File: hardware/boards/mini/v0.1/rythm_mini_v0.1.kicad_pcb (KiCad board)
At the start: 8 copper layers, 18 x 50 mm, 62 parts, among them IC1 NAU88C22YG, IC2 IS42S32160F-6BLI, U1 W25Q128JVP, U2 LTV-217-G, U3 RythmMini, U7 STM32H750IBKx, Y2 Crystal_GND24

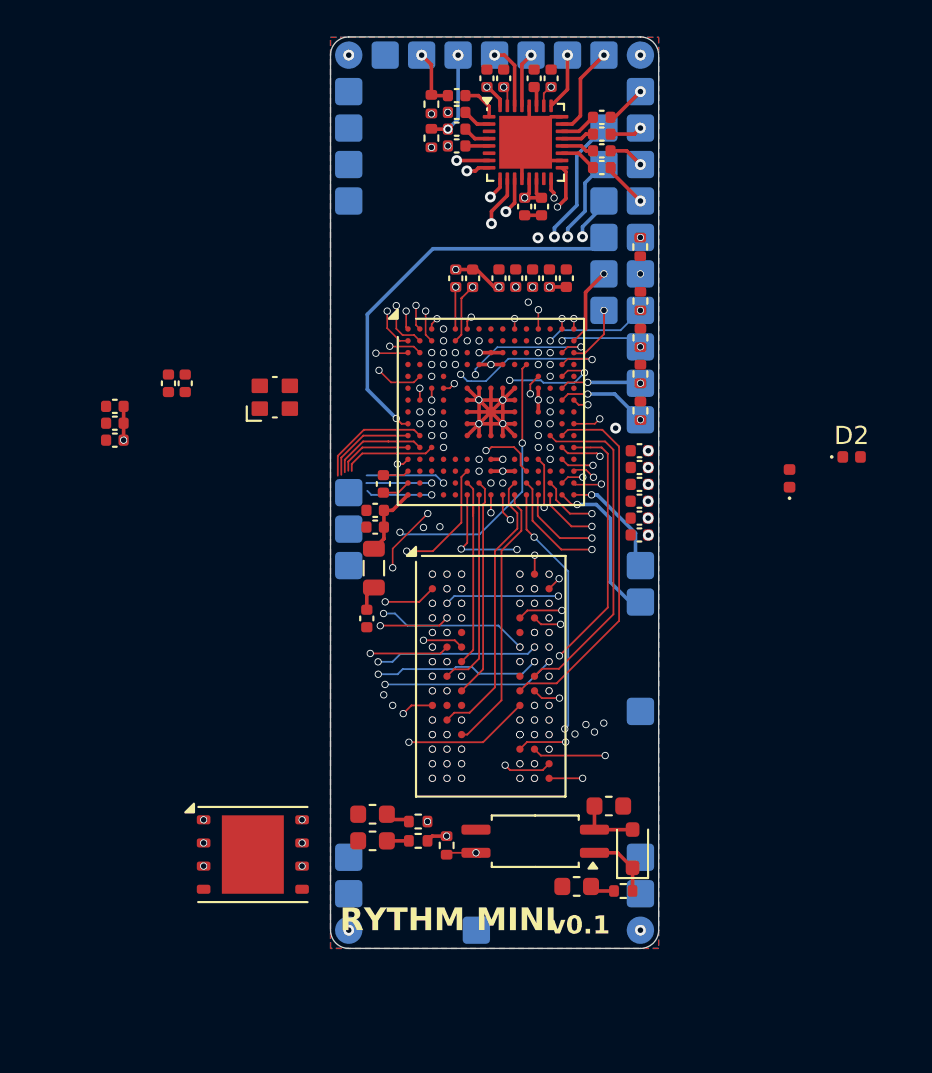
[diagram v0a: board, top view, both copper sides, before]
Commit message: mini: route qspi flash and add more brakeout pads
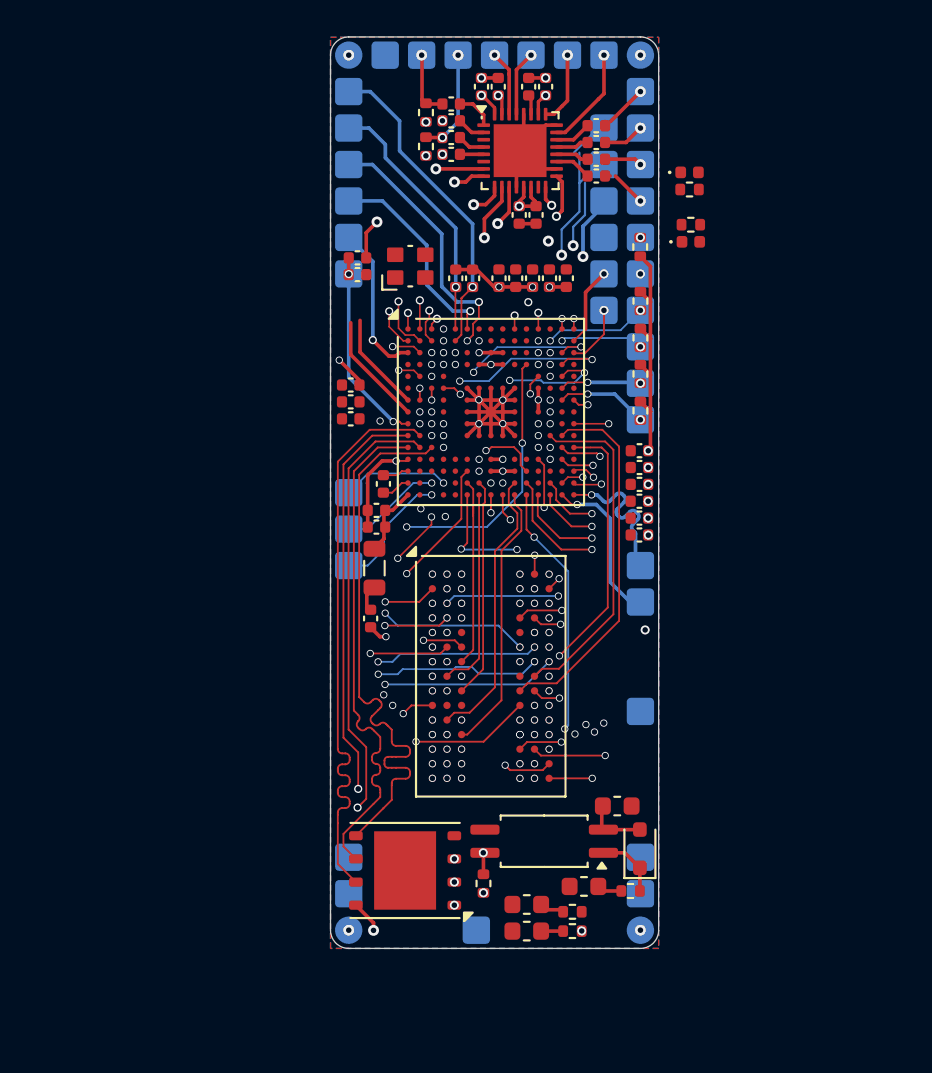
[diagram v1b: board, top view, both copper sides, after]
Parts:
- added R15: R, Resistor_SMD:R_0402_1005Metric, F.Cu at (90.7, 63.4)
- added R16: R, Resistor_SMD:R_0402_1005Metric, F.Cu at (90.8, 65.3)
- moved D2 18.0 mm to (90.7, 62.4)
- moved D1 14.1 mm to (90.8, 66.2), turned to 0 degrees
- moved C2 13.0 mm to (72.1, 74.1)
- moved C6 13.0 mm to (72.1, 75.0)
- moved C9 13.0 mm to (72.1, 76.0)
- moved C33 12.0 mm to (72.5, 68.0), turned to 0 degrees
- moved R5 11.7 mm to (72.5, 67.1), turned to 180 degrees
- moved Y2 10.3 mm to (75.4, 67.6)
- moved FB4 9.80 mm to (81.8, 102.6)
- moved FB5 9.80 mm to (81.8, 104.0)
- moved R9 9.80 mm to (84.3, 104.0), turned to 0 degrees
- moved R8 9.80 mm to (84.3, 103.0)
- moved U1 8.40 mm to (75.1, 100.7), turned to 180 degrees
- moved R6 2.91 mm to (79.4, 101.4), turned to 90 degrees
- moved C19 0.55 mm to (81.3, 64.8)
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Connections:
- D1 pad 2: unconnected-(D1-A-Pad2) -> Net-(D1-A)
- D2 pad 2: unconnected-(D2-A-Pad2) -> Net-(D2-A)
- U3 pad F8: /RST -> (no net)
- U3 pad Y1: unconnected-(U3-GND-PadY1) -> GND
- U7 pad A6: /PB5/RX -> /PB5
- U7 pad B6: /PB6/TX -> /PB6
- U7 pad P3: /PA6/MISO -> /PA6
- U7 pad P4: /PA5/SCK -> /PA5
- U7 pad R3: /PA7/MOSI -> /PA7
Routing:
- net /QSPI_NCS: track 1.53 -> 34.1 mm
- net /QSPI_IO0: track 5.14 -> 31.5 mm
- net /QSPI_IO1: track 5.35 -> 30.9 mm, vias 1 -> 2
- net /QSPI_IO3: track 6.32 -> 31.4 mm, vias 1 -> 0
- net /QSPI_IO2: track 5.20 -> 29.3 mm, vias 1 -> 2
- net /QSPI_CLK: track 4.14 -> 28.0 mm, vias 1 -> 0
- net +3.3V: track 16.9 -> 35.6 mm
- net /PB6: track 0.00 -> 14.4 mm, vias 0 -> 2
- net /I2C_SDA: track 12.3 -> 26.5 mm
- net /I2C_SCL: track 10.9 -> 22.5 mm
- net /PB5: track 0.00 -> 11.5 mm, vias 0 -> 1
- net /RST: track 21.9 -> 10.9 mm, vias 1 -> 2
- net GND: track 37.6 -> 45.3 mm, vias 32 -> 37
- net /PA7: track 0.00 -> 6.84 mm, vias 0 -> 1
- net /VBAT: track 1.77 -> 8.57 mm
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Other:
- board text removed: "RYTHM MINI"
- board text removed: "v0.1"

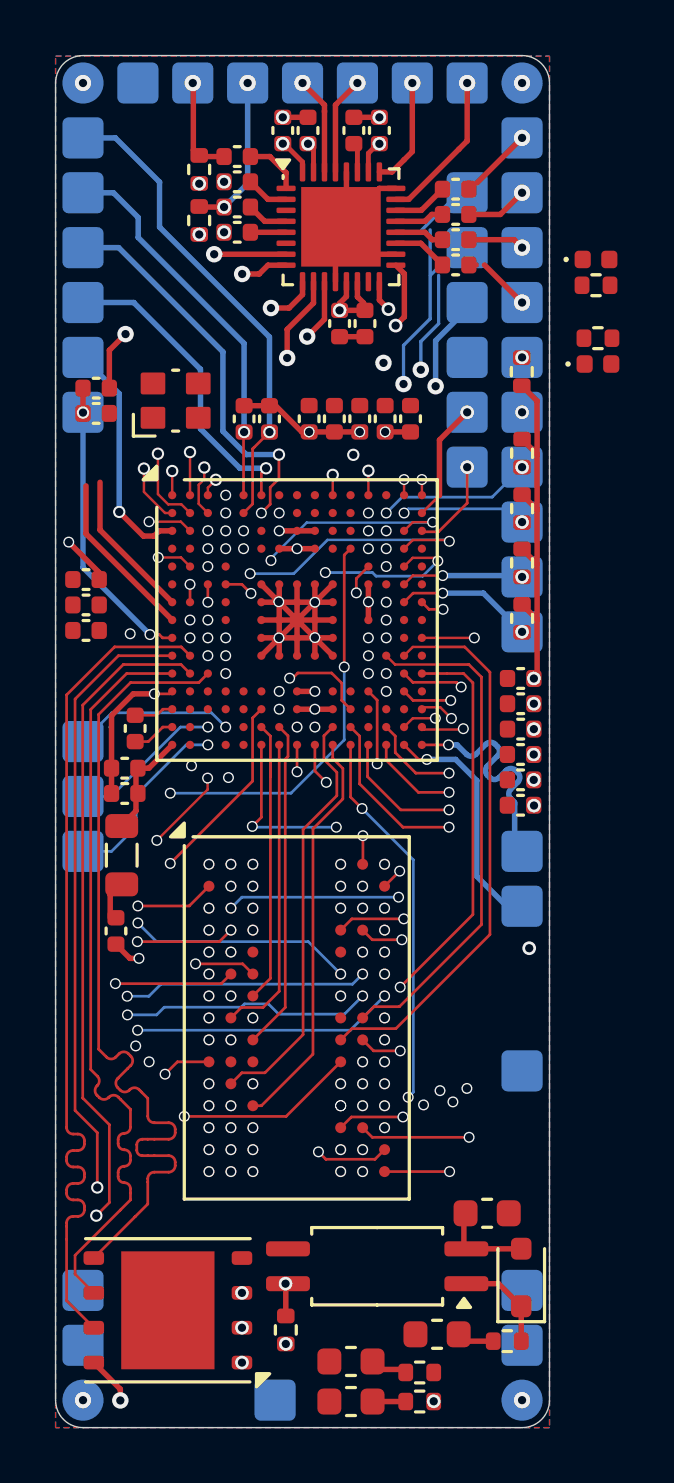
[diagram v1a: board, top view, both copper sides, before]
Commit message: re-routing audio codec
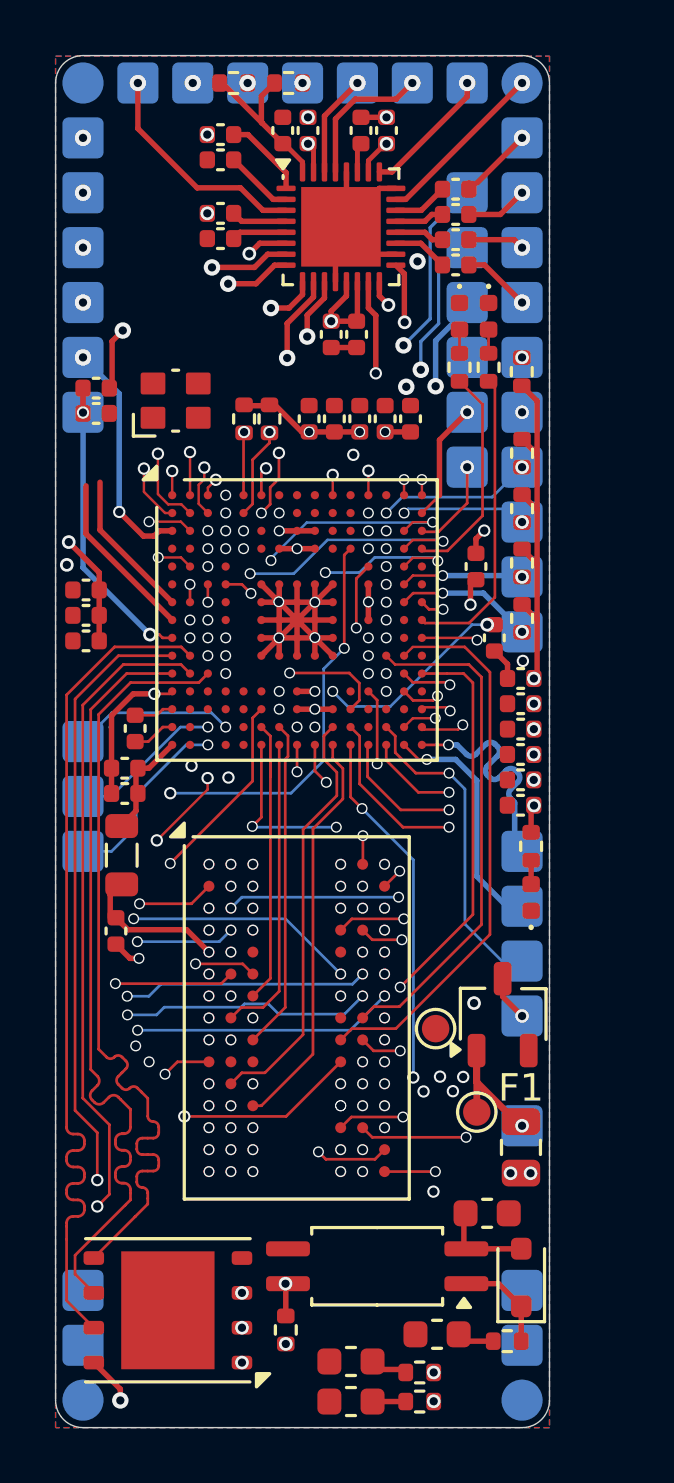
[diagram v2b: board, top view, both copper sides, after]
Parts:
- added C36: 2.2 uF <100 mΩ ESR, Capacitor_SMD:C_0402_1005Metric, F.Cu at (87.0, 76.2)
- added C37: 2.2 uF <100 mΩ ESR, Capacitor_SMD:C_0402_1005Metric, F.Cu at (86.3, 73.6)
- added D4: STATUS2, LED_SMD:LED_0402_1005Metric, F.Cu at (85.7, 64.5)
- added F1: Polyfuse, Fuse:Fuse_0805_2012Metric, F.Cu at (88.0, 94.8)
- added Q1: PMV37EN22, Package_TO_SOT_SMD:TSOT-23, F.Cu at (87.3, 90.0)
- added R17: R, Resistor_SMD:R_0402_1005Metric, F.Cu at (85.7, 66.4)
- added TP1: GND, TestPoint:TestPoint_Pad_D1.0mm, F.Cu at (84.8, 90.5)
- added TP2: 3v3, TestPoint:TestPoint_Pad_D1.0mm, F.Cu at (86.3, 93.5)
- R1, R2: footprint Capacitor_SMD:C_0402_1005Metric -> Resistor_SMD:R_0402_1005Metric
- U3: footprint Library:RythmMini -> Rythm:RythmMini-v0.1
- moved D1 19.6 mm to (88.3, 85.7), turned to 90 degrees
- moved R16 18.7 mm to (88.3, 83.8), turned to -90 degrees
- moved R3 5.97 mm to (79.5, 56.0), turned to 180 degrees
- moved R15 4.93 mm to (86.8, 66.4), turned to 90 degrees
- moved D2 4.43 mm to (86.8, 64.5), turned to -90 degrees
- moved R4 3.39 mm to (77.5, 56.0), turned to 180 degrees
- moved C23 1.01 mm to (77.0, 58.8)
- moved C22 1.01 mm to (77.0, 57.9)
- moved C25 0.65 mm to (77.0, 61.7)
- moved C24 0.65 mm to (77.0, 60.8)
- moved C18 0.50 mm to (82.0, 65.2)
- moved C19 0.50 mm to (81.0, 65.2)
- moved C6 0.38 mm to (72.1, 75.4)
- moved C2 0.38 mm to (72.1, 74.5)
- moved C9 0.38 mm to (72.1, 76.3)
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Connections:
- D1 pad 1: unconnected-(D1-K-Pad1) -> GND
- D2 pad 1: unconnected-(D2-K-Pad1) -> GND
- IC1 pad 3: unconnected-(IC1-LLIN/GPIO2-Pad3) -> /LIN
- IC1 pad 6: unconnected-(IC1-RLIN/GPIO3-Pad6) -> /RIN
- R15 pad 1: unconnected-(R15-Pad1) -> /LED_STATUS
- R16 pad 1: unconnected-(R16-Pad1) -> +3.3V
- U3 pad A1: GND -> unconnected-(U3-NC-PadA1)
- U3 pad A3: /MICL -> /RIN
- U3 pad A4: /MICR -> /MICL
- U3 pad A5: /HPL -> /MICR
- U3 pad A6: /HPR -> /HPL
- U3 pad A7: /SPKL -> /HPR
- U3 pad A8: /SPKR -> /SPKL
- U3 pad A9: GND -> /SPKR
- U3 pad Y1: GND -> unconnected-(U3-NC-PadY1)
- U3 pad Y9: GND -> unconnected-(U3-NC-PadY9)
- U7 pad D15: unconnected-(U7-PA10-PadD15) -> /LED_STATUS2
- U7 pad F13: unconnected-(U7-VCAP-PadF13) -> Net-(C37-Pad1)
- U7 pad H15: unconnected-(U7-PC6-PadH15) -> /LED_STATUS
- U7 pad M10: unconnected-(U7-VCAP-PadM10) -> Net-(C36-Pad1)
- Y2 pad 2: unconnected-(Y2-Pad2) -> GND
- Y2 pad 4: unconnected-(Y2-Pad4) -> GND
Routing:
- net /LED_STATUS: track 0.00 -> 11.1 mm
- net /RIN: track 0.00 -> 9.08 mm, vias 0 -> 2
- net /PB13: track 3.34 -> 11.7 mm
- net +3.3V: track 35.6 -> 43.9 mm, vias 40 -> 43
- net /LIN: track 0.00 -> 8.29 mm, vias 0 -> 1
- net /LED_STATUS2: track 0.00 -> 8.02 mm
- net Net-(C36-Pad1): track 0.00 -> 7.35 mm, vias 0 -> 2
- net /3v3+: track 0.00 -> 5.78 mm, vias 0 -> 1
- net Net-(C37-Pad1): track 0.00 -> 4.53 mm, vias 0 -> 2
- net unconnected-(IC1-CSB/GPIO1-Pad15): track 0.00 -> 3.45 mm, vias 0 -> 1
- net /QSPI_IO0: track 31.5 -> 29.3 mm
- net /HPR: track 3.57 -> 5.27 mm
- net /3v3_GND: track 0.00 -> 1.65 mm, vias 0 -> 1
- net /DIN_MIDI_TX: track 27.6 -> 26.4 mm, vias 1 -> 3
- net /MICL: track 3.67 -> 2.49 mm, vias 1 -> 2
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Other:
- board text added: "3.3v"
- board text added: "CK|PA12"
- board text added: "CMD"
- board text added: "D+"
- board text added: "D-"
- board text added: "D0"
- board text added: "D1"
- board text added: "D2"
- board text added: "D3|PA11"
- board text added: "GND"
- board text added: "PB13"
- board text added: "PB5"
- board text added: "PB6"
- board text added: "RST"
- board text added: "SCL"
- board text added: "SDA"
- board text added: "SDMMC"
- board text added: "VBAT"
- board text removed: "https://www.masach.com/media/catalog/product/file/MS423-10.pdf"

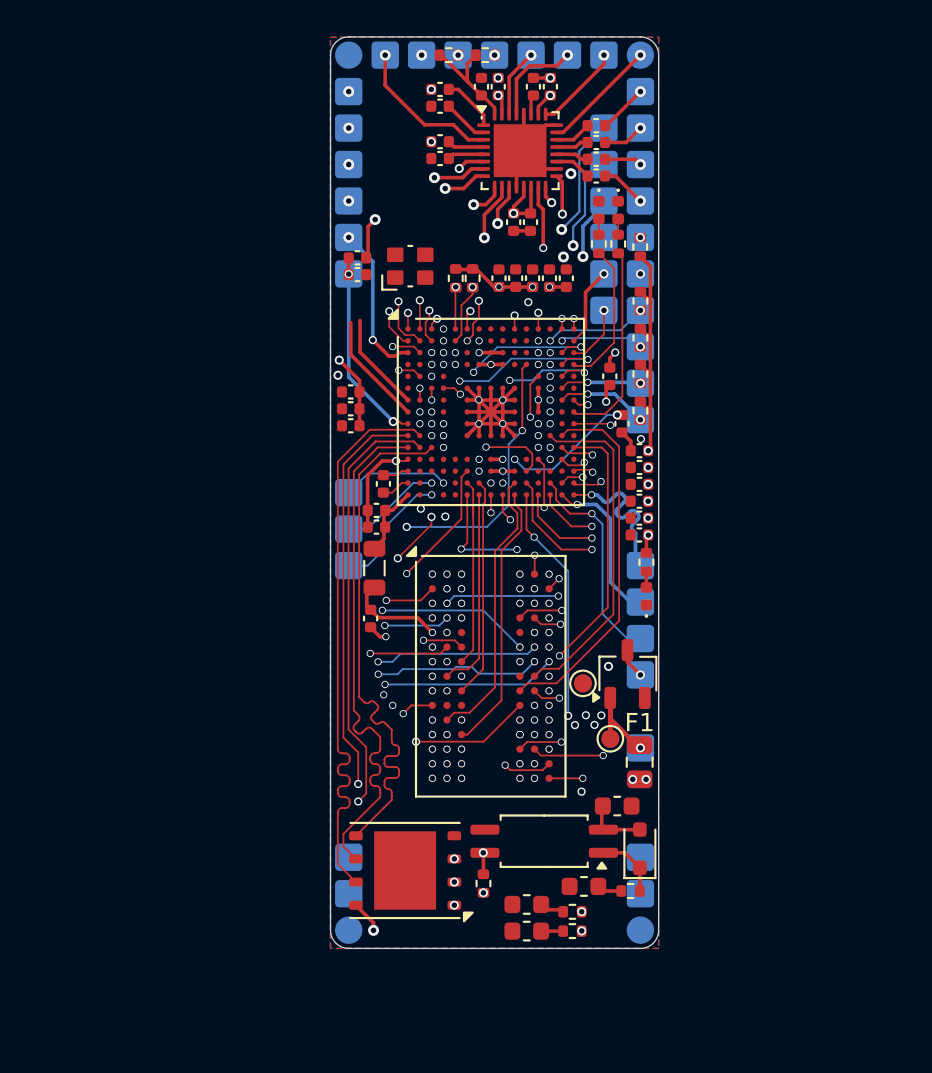
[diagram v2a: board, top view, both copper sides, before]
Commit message: start adding README.md
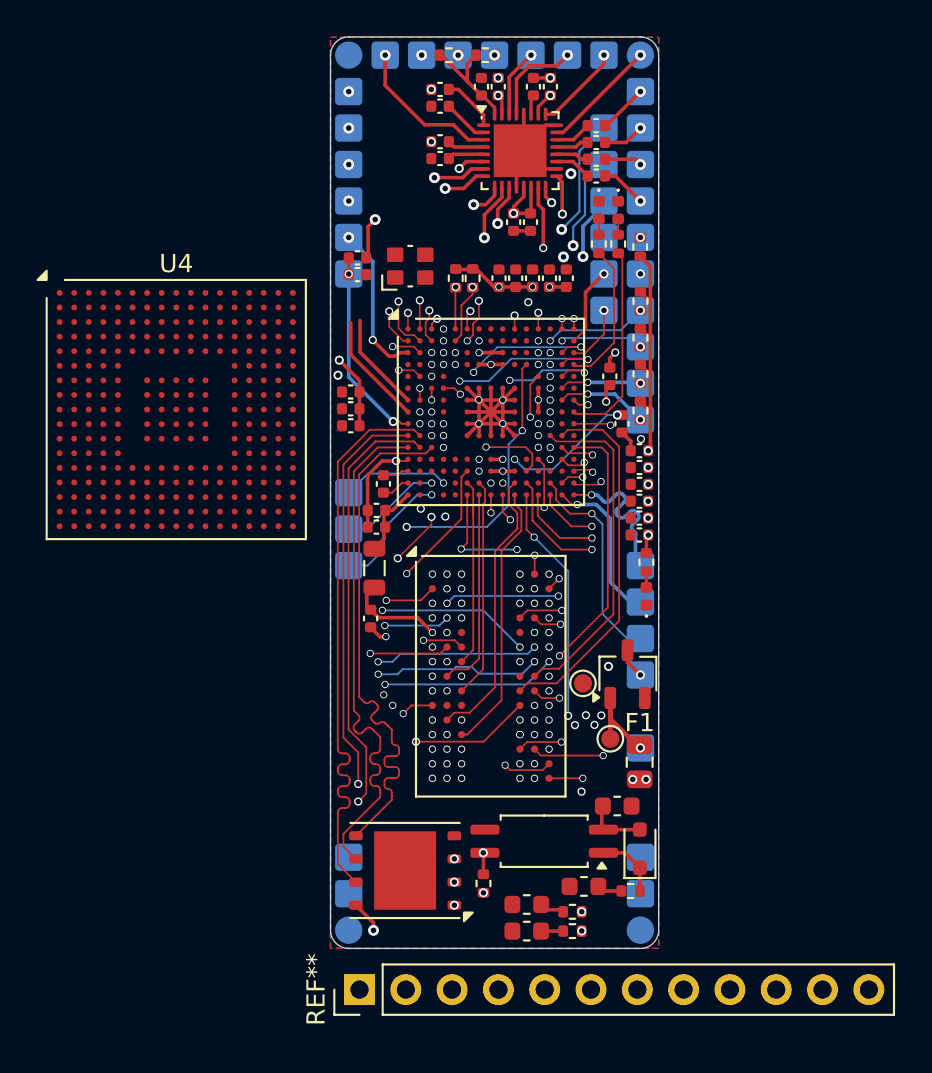
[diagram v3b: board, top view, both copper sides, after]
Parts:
- added REF**: PinHeader_1x12_P2.54mm_Vertical, Connector_PinHeader_2.54mm:PinHeader_1x12_P2.54mm_Vertical, F.Cu at (72.6, 107.3)
- added U4: STM32H750XBHx, Package_BGA:TFBGA-265_14x14mm_Layout17x17_P0.8mm, F.Cu at (62.5, 75.4)
